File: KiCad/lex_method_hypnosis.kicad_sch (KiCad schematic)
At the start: 9 parts, among them J1 Conn_02x05_Odd_Even, J2 Conn_02x05_Odd_Even

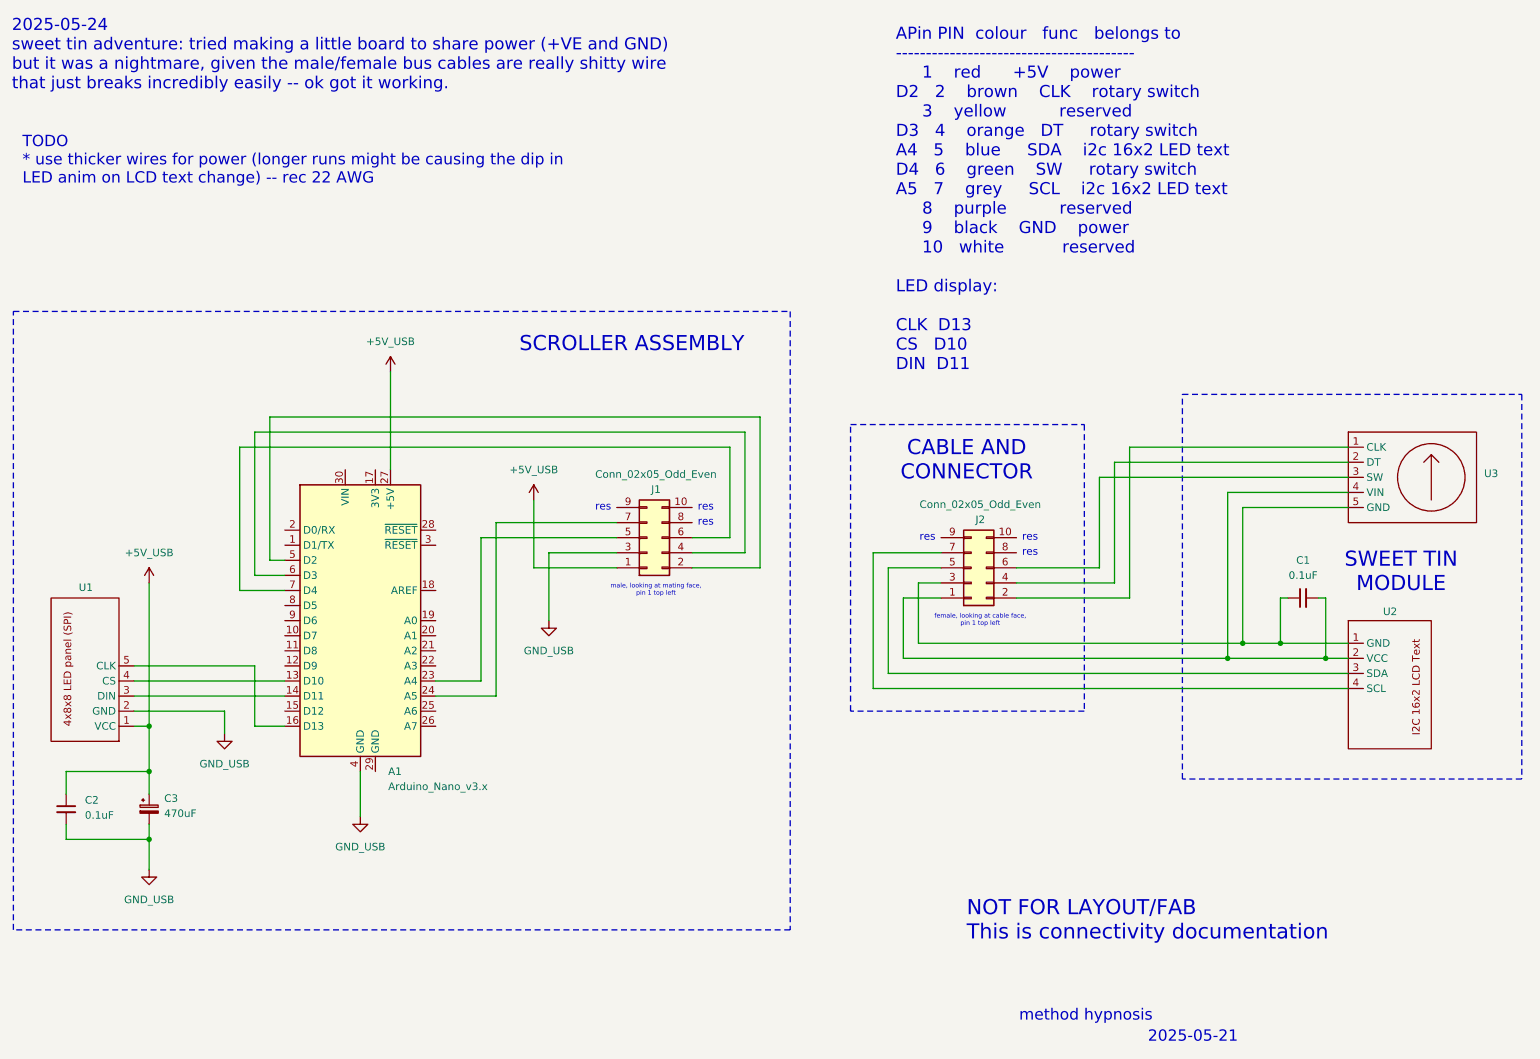
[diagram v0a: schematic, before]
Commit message: Add MCU controlled loading resistor for keeping USB battery supply up when LCD display sleeps
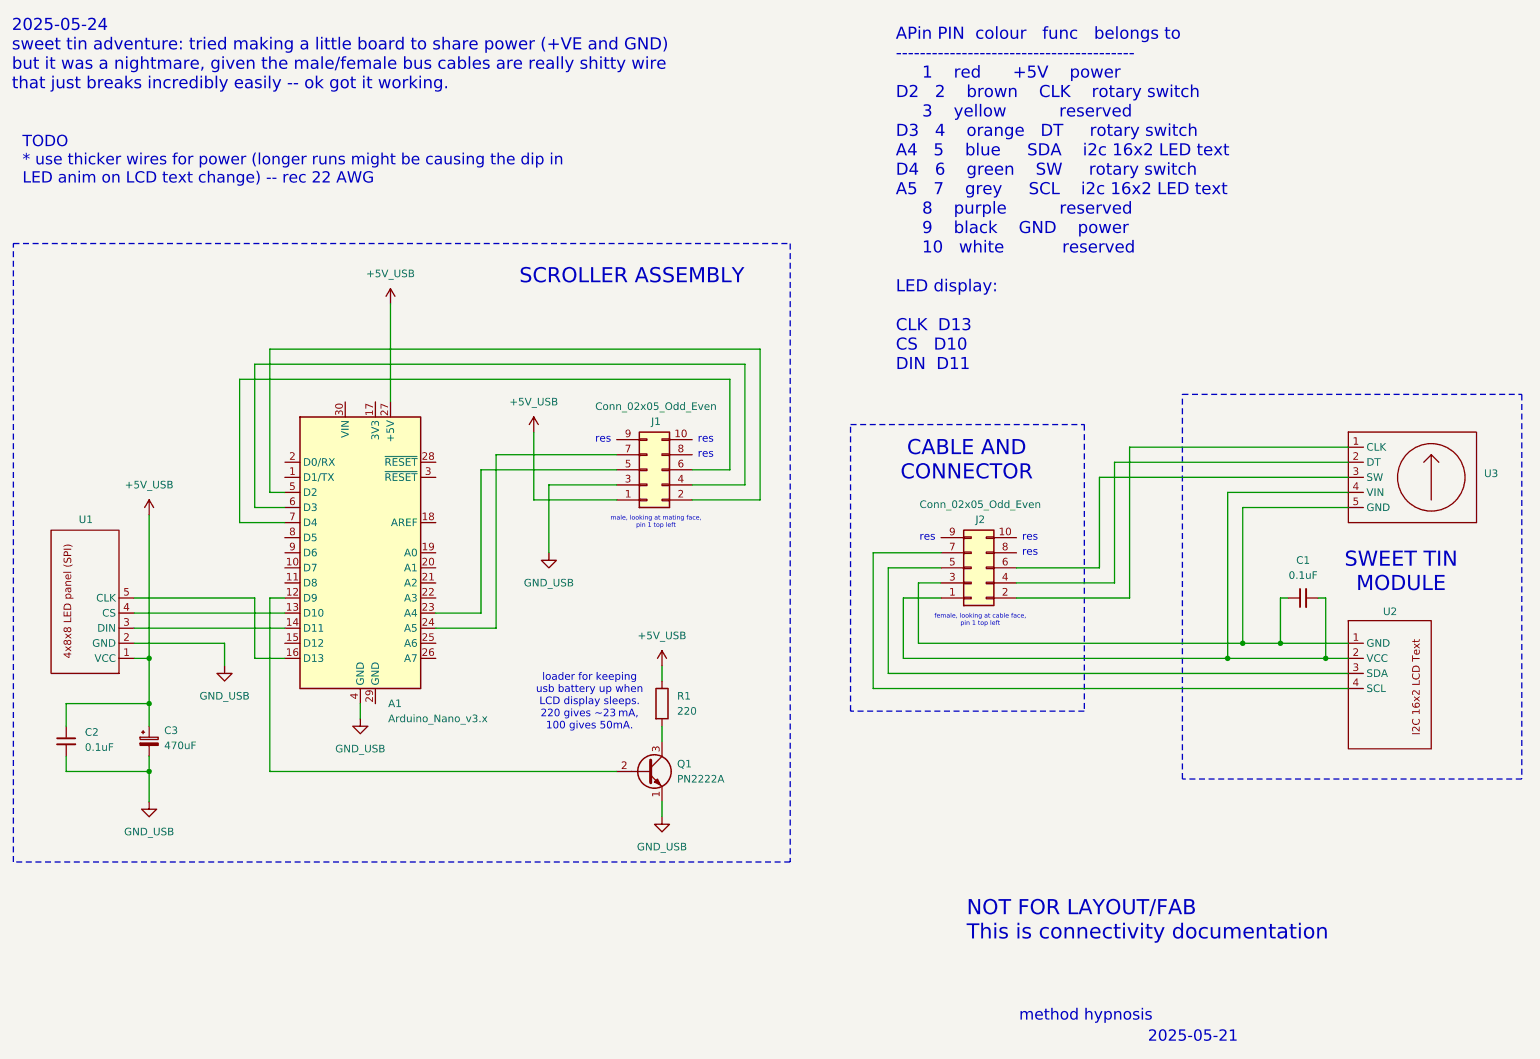
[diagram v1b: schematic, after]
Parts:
- added Q1: PN2222A, Package_TO_SOT_THT:TO-92_Inline, symbol Transistor_BJT:PN2222A
- added R1: 220, symbol Device:R
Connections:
- net +5V_USB: now also R1.1
- net GND_USB: now also Q1.1 (E)
- net at A1.12 (D9): now also Q1.2 (B)
- new net: Q1.3 (C), R1.2
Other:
- note added: "loader for keeping usb battery up when LCD display sleeps. 220 gives ~23 mA, 100 gives 50mA."
- moved on the sheet: A1, C2, C3, J1, U1
